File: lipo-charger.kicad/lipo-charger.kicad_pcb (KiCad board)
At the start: 2 copper layers, 23 x 35 mm, 19 parts, among them J1 JST-PH2 Device, J3 JST-PH2 Bat, SW1 SW_ON, U1 MCP73831-2-OT, U2 XB6166IS

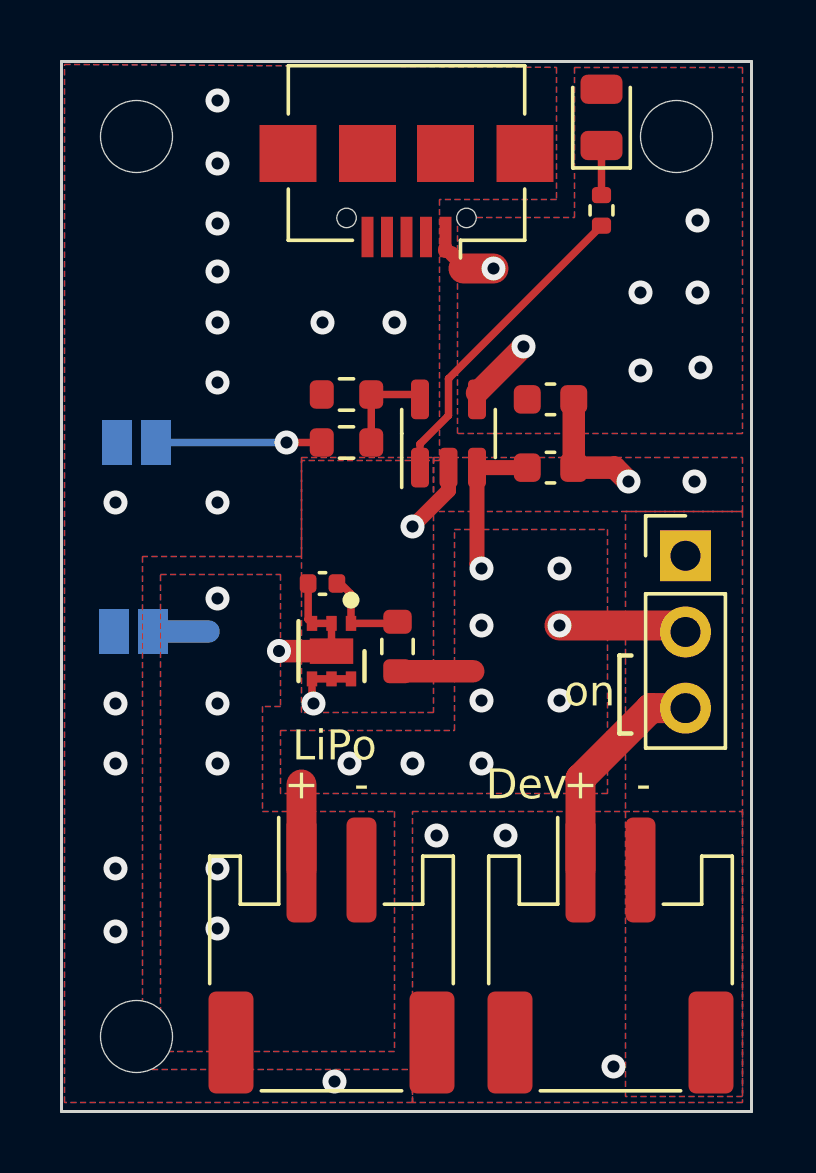
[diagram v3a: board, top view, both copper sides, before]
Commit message: Rev 1.10: added 'always-on' trace-jumper
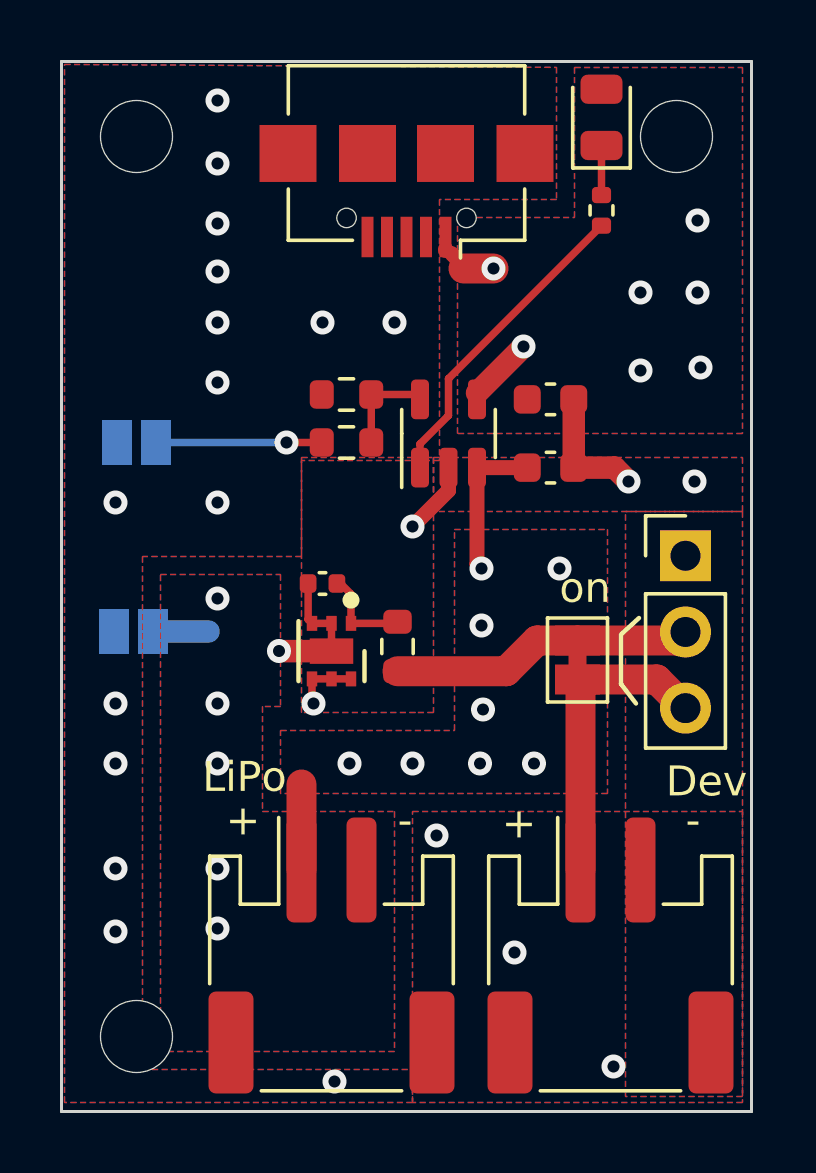
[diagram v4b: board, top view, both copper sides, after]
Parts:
- added JP3: SW_Enable, Jumper:SolderJumper-2_P1.3mm_Bridged_Pad1.0x1.5mm, F.Cu at (117.2, 120.0)
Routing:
- net +BATT: track 14.8 -> 18.1 mm, vias 9 -> 8
- net Net-(J1-Pad1): track 7.52 -> 9.98 mm
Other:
- board text added: "https://github.com/bablokb/ pcb-lipo-charger Rev: 1.10"
- board text removed: "https://github.com/bablokb/ pcb-lipo-charger Rev: 0.93"
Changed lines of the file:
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@@
     )
+  )
+  (footprint "Jumper:SolderJumper-2_P1.3mm_Bridged_Pad1.0x1.5mm" (layer "F.Cu")
+    (at 117.2 119.95 90)
+    (descr "SMD Solder Jumper, 1x1.5mm Pads, 0.3mm gap, bridged with 1 copper strip")
+    (tags "net tie solder jumper bridged")
+    (property "Sheetfile" "lipo-charger.kicad_sch")
+    (property "Sheetname" "")
+    (property "exclude_from_bom" "")
+    (attr exclude_from_pos_files exclude_from_bom)
+    (fp_text reference "JP3" (at 0 -1.8 90) (layer "F.SilkS") hide
+      (effects (font (size 1 1) (thickness 0.15)))
+    )
+    (fp_text value "SW_Enable" (at 0 1.9 90) (layer "F.Fab")
+      (effects (font (size 1 1) (thickness 0.15)))
+    )
+    (fp_poly (pts
+        (xy -0.25 -0.3)
+        (xy 0.25 -0.3)
+        (xy 0.25 0.3)
+        (xy -0.25 0.3)
+      ) (layer "F.Cu") (width 0) (fill solid))
+    (fp_line (start -1.4 -1) (end 1.4 -1) (layer "F.SilkS") (width 0.12))
+    (fp_line (start 1.4 -1) (end 1.4 1) (layer "F.SilkS") (width 0.12))
+    (fp_line (start -1.4 1) (end -1.4 -1) (layer "F.SilkS") (width 0.12))
+    (fp_line (start 1.4 1) (end -1.4 1) (layer "F.SilkS") (width 0.12))
+    (fp_line (start -1.65 -1.25) (end -1.65 1.25) (layer "F.CrtYd") (width 0.05))
+    (fp_line (start 1.65 1.25) (end 1.65 -1.25) (layer "F.CrtYd") (width 0.05))
+    (fp_line (start 1.65 1.25) (end -1.65 1.25) (layer "F.CrtYd") (width 0.05))
+    (fp_line (start -1.65 -1.25) (end 1.65 -1.25) (layer "F.CrtYd") (width 0.05))
+    (pad "1" smd rect (at -0.65 0 90) (size 1 1.5) (layers "F.Cu" "F.Mask")
+      (net 13 "Net-(J1-Pad1)") (pinfunction "A") (pintype "passive"))
+    (pad "2" smd rect (at 0.65 0 90) (size 1 1.5) (layers "F.Cu" "F.Mask")
+      (net 3 "+BATT") (pinfunction "B") (pintype "passive"))
   )
   (footprint "user:MountingHole_2.4mm_M2" (layer "F.Cu")
@@
       (net 7 "Net-(JP1-Pad2)") (pinfunction "B") (pintype "passive"))
   )
-  (gr_line (start 118.6 119.8) (end 118.6 122.4) (layer "F.SilkS") (width 0.15))
-  (gr_line (start 118.6 122.4) (end 119 122.4) (layer "F.SilkS") (width 0.15))
-  (gr_line (start 118.6 119.8) (end 119 119.8) (layer "F.SilkS") (width 0.15))
+  (gr_line (start 118.65 120.75) (end 118.65 119.15) (layer "F.SilkS") (width 0.15))
+  (gr_line (start 119.25 118.55) (end 118.65 119.1) (layer "F.SilkS") (width 0.15))
+  (gr_line (start 119.15 121.4) (end 118.65 120.75) (layer "F.SilkS") (width 0.15))
   (gr_line (start 100 100) (end 123 100) (layer "Edge.Cuts") (width 0.1))
   (gr_line (start 123 100) (end 123 135) (layer "Edge.Cuts") (width 0.1))
   (gr_line (start 100 135) (end 100 100) (layer "Edge.Cuts") (width 0.1))
   (gr_line (start 123 135) (end 100 135) (layer "Edge.Cuts") (width 0.1))
-  (gr_text "https://github.com/bablokb/\n  pcb-lipo-charger\nRev: 0.93" (at 122.1 107.4) (layer "B.SilkS")
+  (gr_text "https://github.com/bablokb/\n  pcb-lipo-charger\nRev: 1.10" (at 122.1 107.4) (layer "B.SilkS")
     (effects (font (size 0.9 0.9) (thickness 0.15)) (justify left mirror))
   )
@@
     (effects (font (size 1 1) (thickness 0.15)) (justify left mirror))
   )
-  (gr_text "+" (at 108 124.1) (layer "F.SilkS")
-    (effects (font (size 1 1) (thickness 0.15)))
-  )
-  (gr_text "LiPo" (at 109.1 122.8) (layer "F.SilkS")
-    (effects (font (size 1 1) (thickness 0.15)))
-  )
-  (gr_text "Dev" (at 115.5 124.1) (layer "F.SilkS")
-    (effects (font (size 1 1) (thickness 0.15)))
-  )
-  (gr_text "on" (at 117.6 121) (layer "F.SilkS")
-    (effects (font (size 1 1) (thickness 0.15)))
-  )
-  (gr_text "-" (at 119.4 124.1) (layer "F.SilkS")
-    (effects (font (size 1 1) (thickness 0.15)))
-  )
-  (gr_text "-" (at 110 124.1) (layer "F.SilkS")
-    (effects (font (size 1 1) (thickness 0.15)))
-  )
-  (gr_text "+" (at 117.3 124.1) (layer "F.SilkS")
+  (gr_text "+" (at 106.05 125.3) (layer "F.SilkS")
+    (effects (font (size 1 1) (thickness 0.15)))
+  )
+  (gr_text "LiPo" (at 106.1 123.85) (layer "F.SilkS")
+    (effects (font (size 1 1) (thickness 0.15)))
+  )
+  (gr_text "Dev" (at 121.5 124) (layer "F.SilkS")
+    (effects (font (size 1 1) (thickness 0.15)))
+  )
+  (gr_text "on" (at 117.45 117.55) (layer "F.SilkS")
+    (effects (font (size 1 1) (thickness 0.15)))
+  )
+  (gr_text "-" (at 121.05 125.3) (layer "F.SilkS")
+    (effects (font (size 1 1) (thickness 0.15)))
+  )
+  (gr_text "-" (at 111.45 125.3) (layer "F.SilkS")
+    (effects (font (size 1 1) (thickness 0.15)))
+  )
+  (gr_text "+" (at 115.25 125.4) (layer "F.SilkS")
     (effects (font (size 1 1) (thickness 0.15)))
   )
@@
   (via (at 108.4 121.4) (size 0.8) (drill 0.4) (layers "F.Cu" "B.Cu") (net 2))
   (via (at 101.8 123.4) (size 0.8) (drill 0.4) (layers "F.Cu" "B.Cu") (free) (net 2))
-  (via (at 114.8 125.8) (size 0.8) (drill 0.4) (layers "F.Cu" "B.Cu") (free) (net 2))
+  (via (at 115.1 129.7) (size 0.8) (drill 0.4) (layers "F.Cu" "B.Cu") (free) (net 2))
   (segment (start 113.85 116.75) (end 114 116.9) (width 0.5) (layer "F.Cu") (net 3))
-  (segment (start 111.2 120.325) (end 113.725 120.325) (width 0.75) (layer "F.Cu") (net 3))
+  (segment (start 117.2 119.3) (end 115.85 119.3) (width 1) (layer "F.Cu") (net 3))
   (segment (start 113.85 113.5375) (end 115.525 113.5375) (width 0.5) (layer "F.Cu") (net 3))
-  (segment (start 120.585 118.8) (end 120.8 119.015) (width 1) (layer "F.Cu") (net 3))
+  (segment (start 120.515 119.3) (end 120.8 119.015) (width 1) (layer "F.Cu") (net 3))
+  (segment (start 114.825 120.325) (end 111.2 120.325) (width 1) (layer "F.Cu") (net 3))
   (segment (start 108 126.95) (end 108 124.1) (width 1) (layer "F.Cu") (net 3))
-  (segment (start 116.6 118.8) (end 120.585 118.8) (width 1) (layer "F.Cu") (net 3))
+  (segment (start 115.85 119.3) (end 114.825 120.325) (width 1) (layer "F.Cu") (net 3))
+  (segment (start 117.2 119.3) (end 120.515 119.3) (width 1) (layer "F.Cu") (net 3))
   (segment (start 113.85 113.5375) (end 113.85 116.75) (width 0.5) (layer "F.Cu") (net 3))
   (via (at 109.6 123.4) (size 0.8) (drill 0.4) (layers "F.Cu" "B.Cu") (free) (net 3))
   (via (at 114 116.9) (size 0.8) (drill 0.4) (layers "F.Cu" "B.Cu") (free) (net 3))
   (via (at 116.6 116.9) (size 0.8) (drill 0.4) (layers "F.Cu" "B.Cu") (free) (net 3))
-  (via (at 114 121.3) (size 0.8) (drill 0.4) (layers "F.Cu" "B.Cu") (free) (net 3))
-  (via (at 116.6 121.3) (size 0.8) (drill 0.4) (layers "F.Cu" "B.Cu") (free) (net 3))
-  (via (at 114 123.4) (size 0.8) (drill 0.4) (layers "F.Cu" "B.Cu") (free) (net 3))
-  (via (at 116.6 118.8) (size 0.8) (drill 0.4) (layers "F.Cu" "B.Cu") (free) (net 3))
+  (via (at 114.05 121.6) (size 0.8) (drill 0.4) (layers "F.Cu" "B.Cu") (free) (net 3))
+  (via (at 115.75 123.4) (size 0.8) (drill 0.4) (layers "F.Cu" "B.Cu") (free) (net 3))
+  (via (at 113.95 123.4) (size 0.8) (drill 0.4) (layers "F.Cu" "B.Cu") (free) (net 3))
   (via (at 111.7 123.4) (size 0.8) (drill 0.4) (layers "F.Cu" "B.Cu") (free) (net 3))
   (via (at 114 118.8) (size 0.8) (drill 0.4) (layers "F.Cu" "B.Cu") (free) (net 3))
@@
   (segment (start 111.95 112.75) (end 112.9 111.8) (width 0.25) (layer "F.Cu") (net 9))
   (segment (start 111.95 113.5375) (end 111.95 112.75) (width 0.25) (layer "F.Cu") (net 9))
-  (segment (start 119.645 121.555) (end 120.8 121.555) (width 1) (layer "F.Cu") (net 13))
-  (segment (start 117.3 123.9) (end 119.645 121.555) (width 1) (layer "F.Cu") (net 13))
-  (segment (start 117.3 126.95) (end 117.3 123.9) (width 1) (layer "F.Cu") (net 13))
+  (segment (start 117.3 126.95) (end 117.3 120.9625) (width 1) (layer "F.Cu") (net 13))
+  (segment (start 117.2 120.6) (end 119.845 120.6) (width 1) (layer "F.Cu") (net 13))
+  (segment (start 119.845 120.6) (end 120.8 121.555) (width 1) (layer "F.Cu") (net 13))
   (zone (net 3) (net_name "+BATT") (layers F&B.Cu) (hatch edge 0.508)
     (connect_pads (clearance 0.508))
